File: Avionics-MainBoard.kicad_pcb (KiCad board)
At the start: 4 copper layers, 90.2 x 95.9 mm, 270 parts, among them J1 USB_C_Receptacle_USB2.0, J10 1824543, J11 1824527, J12 1824527, J13 1824527, J14 200528-0100, J15 200528-0100, J16 200528-0100, J17 1824543, J18 200528-0100, J19 200528-0100, J2 200528-0100, J3 Conn_01x06, J4 200528-0100, J5 Micro_SD_Card_Det2, J6 200528-0100, J7 U.FL-R-SMT-1, J8 Conn_01x02, J9 200528-0100, Q1 IRLML2803, Q10 MBT2222ADW1T1, Q11 MBT2222ADW1T1, Q12 MBT2222ADW1T1, Q13 MBT2222ADW1T1, Q14 MMBT2907, Q15 MMBT2907, Q16 NX3008NBKS, Q17 MBT2222ADW1T1, Q2 MBT2222ADW1T1, Q22 NX3008NBKS, Q24 NX3008NBKS, Q26 NX3008NBKS, Q28 NX3008NBKS, Q29 MBT2222ADW1T1, Q3 MBT2222ADW1T1, Q30 MBT2222ADW1T1, Q4 NX3008NBKS, Q44 NX3008NBKS, Q46 NX3008NBKS, Q48 NX3008NBKS, Q5 MBT2222ADW1T1, Q50 NX3008NBKS, Q52 NX3008NBKS, Q6 MBT2222ADW1T1, Q7 MBT2222ADW1T1, Q8 MBT2222ADW1T1, Q9 MBT2222ADW1T1, Q99 NX3008NBKS, SW1 SW_Omron_B3FS, SW2 SW_Omron_B3FS, U1 MR25H40MDF, U10 BTS5090-1EJA, U12 ADM1491EBR, U14 ADM1176-1ARMZ-R7, U15 TPS7A4501DCQT, U16 ADM1176-1ARMZ-R7, U17 TPS54226PWPR, U18 ADM1176-1ARMZ-R7, U2 RP2040, U3 MAX706RESA+, U4 DS3231M, U5 BNO085, U6 USBLC6-2SC6, U7 E22-900M30S, U8 S1216V8, U9 BQ25883RGER, Y1 12MHz, Y2 32.768kHz

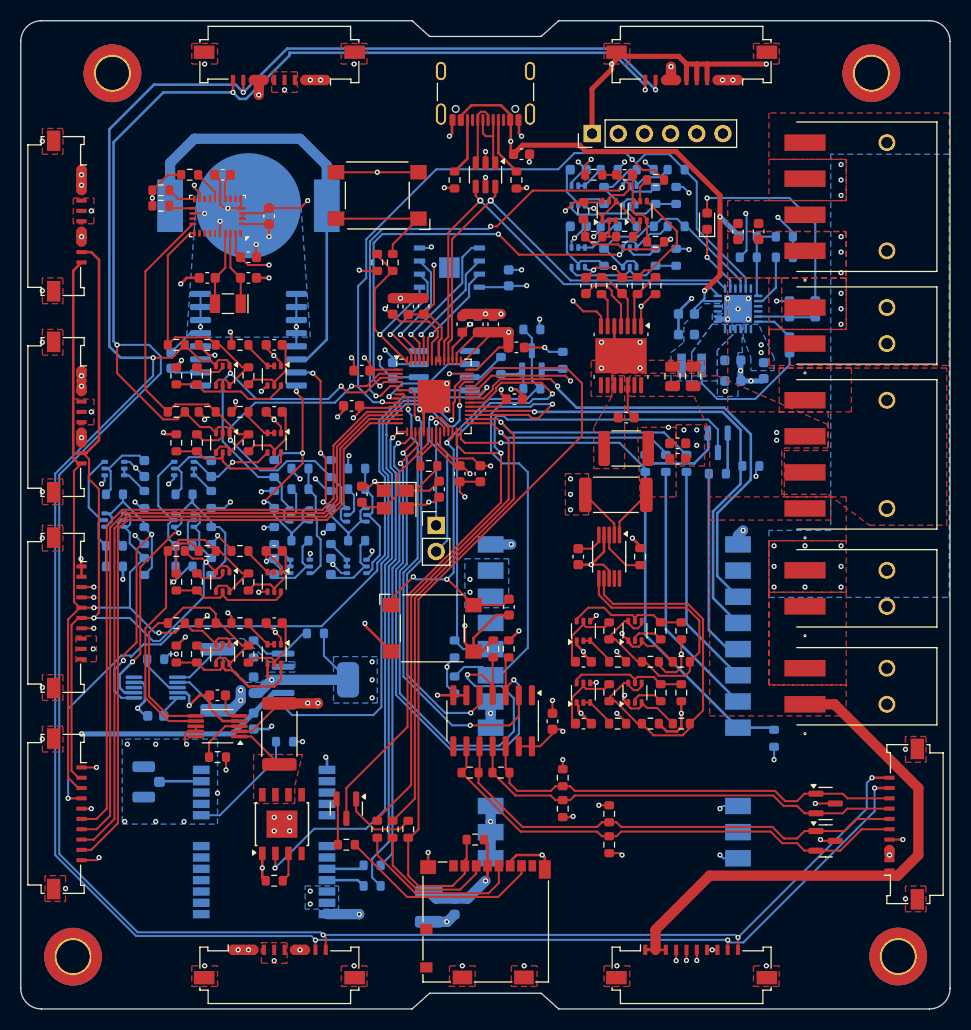
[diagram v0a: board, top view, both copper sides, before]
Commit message: Fixed schematic bugs and corresponding layout modifications
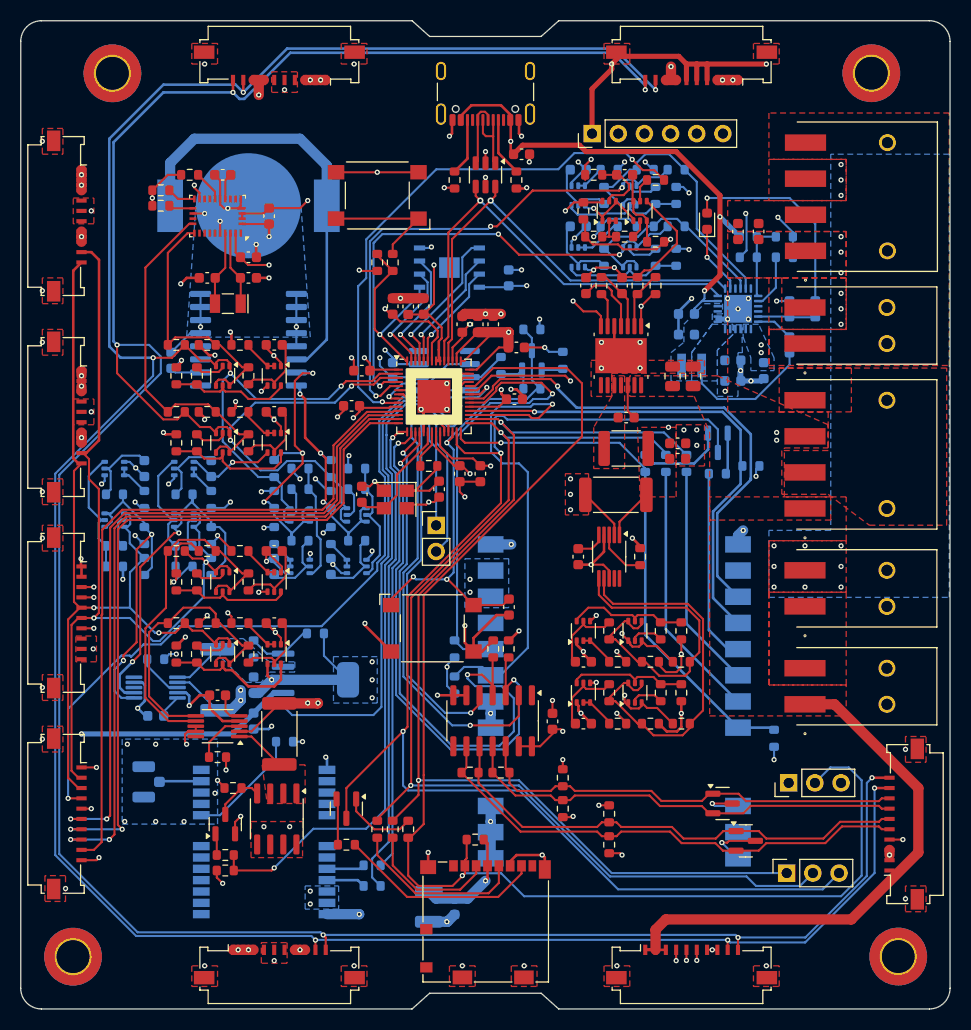
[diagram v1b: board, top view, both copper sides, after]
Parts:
- removed R64: 1k, Resistor_SMD:R_0603_1608Metric
- removed U10: BTS5090-1EJA, Package_SO:Infineon_PG-DSO-8-43
- added J20: Conn_01x03, Connector_PinSocket_2.54mm:PinSocket_1x03_P2.54mm_Vertical, F.Cu at (179.2, 134.8)
- added J21: Conn_01x03, Connector_PinHeader_2.54mm:PinHeader_1x03_P2.54mm_Vertical, F.Cu at (179.4, 126.0)
- added Q18: IRLML0030, Package_TO_SOT_SMD:SOT-23, F.Cu at (124.8, 130.0)
- added Q19: IRF7404, Package_SO:SOIC-8_3.9x4.9mm_P1.27mm, F.Cu at (129.8, 129.5)
- added R36: 10K, Resistor_SMD:R_0603_1608Metric, F.Cu at (124.8, 134.5)
- added R37: 4.7K, Resistor_SMD:R_0603_1608Metric, F.Cu at (124.8, 133.0)
- added R38: 3.3K, Resistor_SMD:R_0603_1608Metric, F.Cu at (125.5, 126.5)
- U4: value DS3231M -> DS3231S
- moved D1 10.0 mm to (173.0, 128.0)
- moved D2 7.75 mm to (175.2, 131.6)
- moved J10 0.05 mm to (181.1, 69.1)
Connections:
- J16 pad 6: /MCU_IO/SPI1_MISO -> /MCU_IO/Jetson_CSn
- J16 pad 7: /MCU_IO/Jetson_CSn -> /MCU_IO/SPI1_MOSI
- J16 pad 9: /MCU_IO/SPI1_MOSI -> /MCU_IO/SPI1_MISO
- J18 pad 10: /MCU_IO/I2C0_SDA -> /MCU_IO/I2C0_SCL
- J18 pad 9: /MCU_IO/I2C0_SCL -> /MCU_IO/I2C0_SDA
- J19 pad 10: /MCU_IO/I2C0_SDA -> /MCU_IO/I2C0_SCL
- J19 pad 9: /MCU_IO/I2C0_SCL -> /MCU_IO/I2C0_SDA
- J2 pad 10: /MCU_IO/I2C0_SDA -> /MCU_IO/I2C0_SCL
- J2 pad 9: /MCU_IO/I2C0_SCL -> /MCU_IO/I2C0_SDA
- J4 pad 10: /MCU_IO/I2C0_SDA -> /MCU_IO/I2C0_SCL
- J4 pad 9: /MCU_IO/I2C0_SCL -> /MCU_IO/I2C0_SDA
- J6 pad 10: /MCU_IO/I2C0_SDA -> /MCU_IO/I2C0_SCL
- J6 pad 9: /MCU_IO/I2C0_SCL -> /MCU_IO/I2C0_SDA
- Q17 pad 1: /MCU_IO/I2C0_SDA -> /MCU_IO/I2C0_SCL
- Q17 pad 3: /MCU_IO/I2C0_SDA -> /MCU_IO/I2C0_SCL
- Q17 pad 4: /RTC/RTC_SDA -> /RTC/RTC_SCL
- Q17 pad 6: /RTC/RTC_SDA -> /RTC/RTC_SCL
- Q3 pad 1: /MCU_IO/I2C0_SCL -> /MCU_IO/I2C0_SDA
- Q3 pad 3: /MCU_IO/I2C0_SCL -> /MCU_IO/I2C0_SDA
- Q5 pad 1: /MCU_IO/I2C0_SCL -> /MCU_IO/I2C0_SDA
- Q5 pad 3: /MCU_IO/I2C0_SCL -> /MCU_IO/I2C0_SDA
- Q5 pad 4: /RTC/RTC_SCL -> /RTC/RTC_SDA
- Q5 pad 6: /RTC/RTC_SCL -> /RTC/RTC_SDA
- Q9 pad 1: /MCU_IO/I2C0_SDA -> /MCU_IO/I2C0_SCL
- Q9 pad 3: /MCU_IO/I2C0_SDA -> /MCU_IO/I2C0_SCL
- R104 pad 1: /RTC/RTC_SDA -> /RTC/RTC_SCL
- R104 pad 2: /MCU_IO/I2C0_SDA -> /MCU_IO/I2C0_SCL
- R15 pad 2: /MCU_IO/I2C0_SDA -> /MCU_IO/I2C0_SCL
- R165 pad 2: /MCU_IO/I2C0_SCL -> /MCU_IO/I2C0_SDA
- R171 pad 1: /RTC/RTC_SCL -> /RTC/RTC_SDA
- R171 pad 2: /MCU_IO/I2C0_SCL -> /MCU_IO/I2C0_SDA
- R173 pad 2: /RTC/RTC_SCL -> /RTC/RTC_SDA
- R174 pad 1: /RTC/RTC_SCL -> /RTC/RTC_SDA
- R97 pad 2: /RTC/RTC_SDA -> /RTC/RTC_SCL
- R98 pad 1: /RTC/RTC_SDA -> /RTC/RTC_SCL
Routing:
- net /MCU_IO/SD_CSn: track 76.9 -> 132.4 mm, vias 0 -> 1
- net /LoRa Power/MISO: track 75.7 -> 128.1 mm, vias 1 -> 2
- net /LoRa Power/CLK: track 63.7 -> 107.3 mm, vias 1 -> 2
- net /LoRa Power/MOSI: track 66.6 -> 106.0 mm, vias 1 -> 2
- net /MCU_IO/I2C0_SCL: track 280.8 -> 291.2 mm
- net Net-(Q18-D): track 0.00 -> 4.95 mm
- net /MCU_IO/I2C0_SDA: track 287.7 -> 283.5 mm
- net /MCU_IO/GPS_EN: track 65.9 -> 70.0 mm
- net /RTC/RTC_SDA: track 26.8 -> 30.6 mm
- net GND: track 348.3 -> 351.8 mm, vias 127 -> 126
- net /MCU_IO/SPI1_CLK: track 67.2 -> 70.2 mm, vias 0 -> 2
- net Net-(U10-DEN): track 2.89 -> 0.00 mm
- net /MCU_IO/SPI1_MISO: track 66.3 -> 69.2 mm
- net Net-(Q18-G): track 0.00 -> 2.11 mm
- net /MCU_IO/SPI1_MOSI: track 67.9 -> 69.8 mm, vias 0 -> 2
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
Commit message: Updated connector locations and types
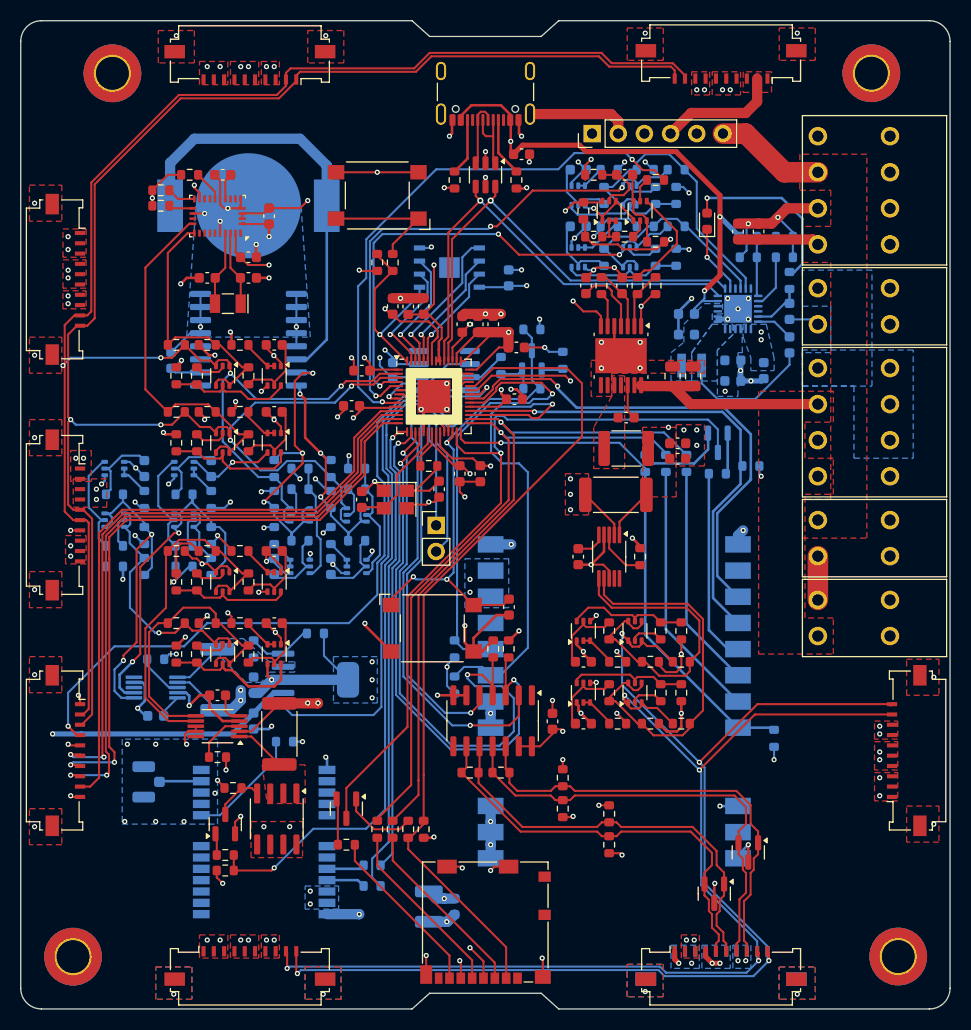
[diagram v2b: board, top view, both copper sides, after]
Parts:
- removed J20: Conn_01x03, Connector_PinSocket_2.54mm:PinSocket_1x03_P2.54mm_Vertical
- removed J21: Conn_01x03, Connector_PinHeader_2.54mm:PinHeader_1x03_P2.54mm_Vertical
- J10, J17: footprint Argus-Connectors:1824543 -> Argus-Connectors:1823654
- J11, J12, J13: footprint Argus-Connectors:1824527 -> Argus-Connectors:1823638
- J14: moved to B.Cu
- moved J14 95.8 mm to (172.9, 143.2), turned to 180 degrees
- moved J19 89.3 mm to (109.8, 77.1), turned to -90 degrees
- moved J2 86.4 mm to (127.1, 143.2), turned to 0 degrees
- moved J9 71.4 mm to (172.9, 56.8), turned to 180 degrees
- moved J18 63.7 mm to (190.4, 122.9), turned to 90 degrees
- moved J4 42.9 mm to (127.1, 56.8)
- moved J6 21.8 mm to (172.9, 143.2), turned to 0 degrees
- moved J15 9.50 mm to (109.8, 100.0)
- moved J16 6.14 mm to (109.8, 122.9)
- moved D2 5.96 mm to (172.2, 136.8), turned to -90 degrees
- moved D1 5.37 mm to (175.5, 132.8), turned to -90 degrees
- moved R48 5.10 mm to (144.0, 130.5), turned to -90 degrees
- moved J13 5.03 mm to (182.2, 111.8)
- moved R70 3.72 mm to (179.5, 77.2)
- moved J12 3.37 mm to (182.2, 104.0)
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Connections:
- J12 pad 3: GNDREF -> GND
- J12 pad 4: GNDREF -> GND
- J13 pad 3: GNDREF -> GND
- J13 pad 4: GNDREF -> GND
- J14 pad 1: VSYS -> /MCU_IO/I2C1_SCL
- J14 pad 10: /MCU_IO/I2C1_SCL -> VSYS
- J14 pad 2: VSYS -> /MCU_IO/I2C1_SDA
- J14 pad 3: VSYS -> +3V3
- J14 pad 4: GND -> +3V3
- J14 pad 7: +3V3 -> GND
- J14 pad 8: +3V3 -> VSYS
- J14 pad 9: /MCU_IO/I2C1_SDA -> VSYS
- J15 pad 5: /MCU_IO/I2C1_SCL -> /MCU_IO/I2C0_SCL
- J15 pad 6: /MCU_IO/I2C1_SDA -> /MCU_IO/I2C0_SDA
- J16 pad 2: /MCU_IO/I2C1_SDA -> /MCU_IO/I2C0_SDA
- J16 pad 3: /MCU_IO/I2C1_SCL -> /MCU_IO/I2C0_SCL
- J18 pad 10: /MCU_IO/I2C0_SCL -> /MCU_IO/I2C1_SCL
- J18 pad 9: /MCU_IO/I2C0_SDA -> /MCU_IO/I2C1_SDA
- J2 pad 10: /MCU_IO/I2C0_SCL -> /MCU_IO/I2C1_SCL
- J2 pad 9: /MCU_IO/I2C0_SDA -> /MCU_IO/I2C1_SDA
- J4 pad 1: VSYS -> /MCU_IO/I2C0_SCL
- J4 pad 10: /MCU_IO/I2C0_SCL -> VSYS
- J4 pad 2: VSYS -> /MCU_IO/I2C0_SDA
- J4 pad 3: VSYS -> +3V3
- J4 pad 4: GND -> +3V3
- J4 pad 7: +3V3 -> GND
- J4 pad 8: +3V3 -> VSYS
- J4 pad 9: /MCU_IO/I2C0_SDA -> VSYS
- J6 pad 10: /MCU_IO/I2C0_SCL -> /MCU_IO/I2C1_SCL
- J6 pad 9: /MCU_IO/I2C0_SDA -> /MCU_IO/I2C1_SDA
- J9 pad 10: /MCU_IO/I2C1_SCL -> /MCU_IO/I2C0_SCL
- J9 pad 9: /MCU_IO/I2C1_SDA -> /MCU_IO/I2C0_SDA
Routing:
- net /MCU_IO/I2C0_SCL: track 291.2 -> 176.2 mm, vias 8 -> 4
- net /MCU_IO/I2C0_SDA: track 283.5 -> 177.6 mm, vias 8 -> 4
- net /LoRa Power/MISO: track 128.1 -> 75.7 mm, vias 2 -> 1
- net /MCU_IO/SD_CSn: track 132.4 -> 81.0 mm, vias 1 -> 0
- net /MCU_IO/I2C1_SCL: track 213.1 -> 263.5 mm, vias 6 -> 8
- net VSYS: track 314.9 -> 364.1 mm, vias 15 -> 13
- net /LoRa Power/CLK: track 107.3 -> 63.7 mm, vias 2 -> 1
- net /LoRa Power/MOSI: track 106.0 -> 66.6 mm, vias 2 -> 1
- net /MCU_IO/I2C1_SDA: track 209.8 -> 238.5 mm, vias 6 -> 8
- net GND: track 351.8 -> 326.8 mm, vias 126 -> 129
- net +3V3: track 186.7 -> 172.7 mm, vias 66 -> 76
- net GNDREF: track 60.6 -> 47.4 mm, vias 17 -> 16
- net /MCU_IO/SPI1_MOSI: track 69.8 -> 62.1 mm
- net /RS485/TX+: track 48.9 -> 41.2 mm
- net /MCU_IO/SPI1_MISO: track 69.2 -> 61.7 mm
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- added copper zone on B.Cu, net +3V3
- added copper zone on B.Cu, net VSYS
- removed copper zone on F.Cu, net GNDREF
- removed copper zone on F.Cu, net Net-(J12-Pad1)
- removed copper zone on B.Cu, net VBATT

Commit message: Added silkscreen
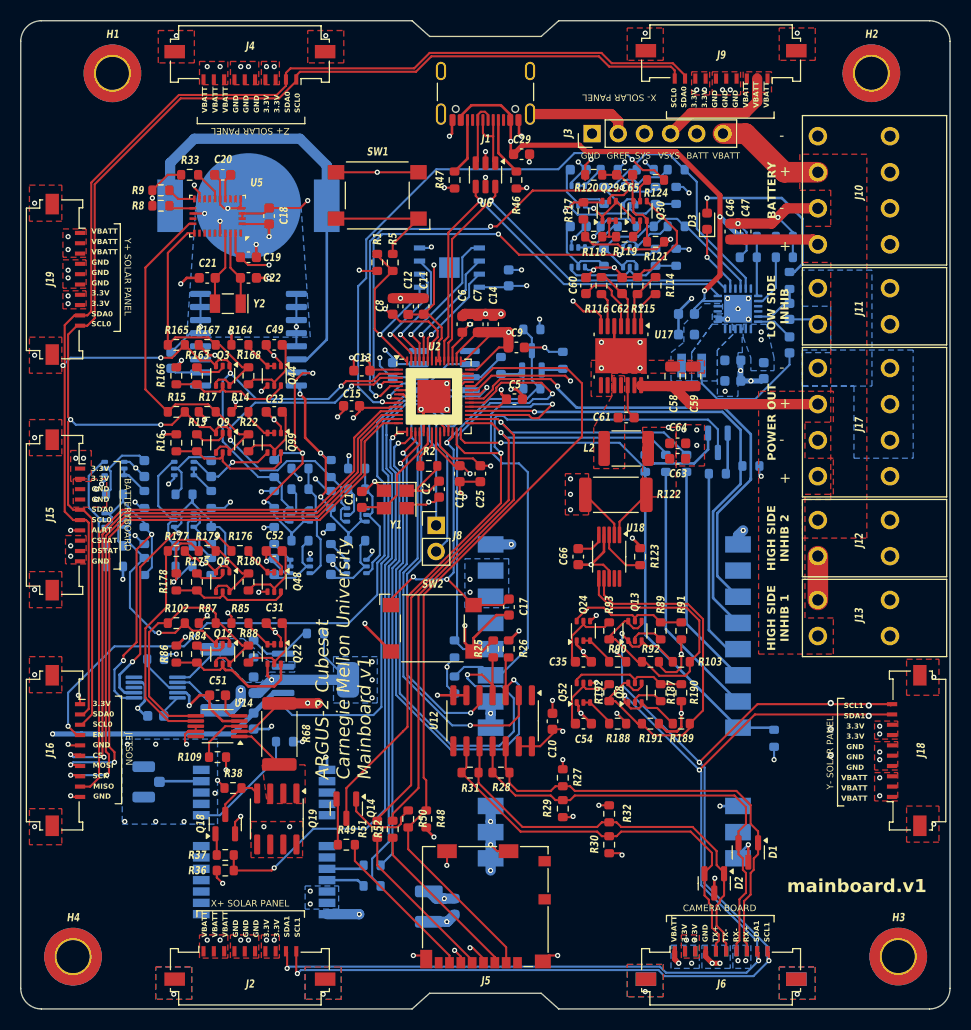
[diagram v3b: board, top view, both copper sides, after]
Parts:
- added REF**: VAL**, mainboard:board_info_block, B.Cu at (111.5, 77.5)
- moved J5 1.50 mm to (150.0, 138.0)
- moved C47 1.25 mm to (175.2, 72.5)
- moved R48 1.03 mm to (144.2, 129.5)
- moved D2 1.00 mm to (172.2, 135.8)
- moved R50 1.00 mm to (142.5, 129.5)
- moved C46 0.75 mm to (173.8, 72.5)
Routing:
- net /SD/SD_CLK: track 17.4 -> 15.7 mm
- net /SD/SD_MOSI: track 17.7 -> 16.2 mm
- net /SD/SD_MISO: track 16.8 -> 15.3 mm
- net +3V3: track 172.7 -> 171.4 mm
- net /MCU_IO/SD_CSn: track 81.0 -> 79.9 mm
- net GNDREF: track 47.4 -> 48.4 mm
- net VBATT: track 18.7 -> 19.5 mm
- net Net-(Q14-B): track 7.30 -> 7.90 mm
- net GND: track 326.8 -> 326.3 mm
- net /MCU_IO/I2C1_SCL: track 263.5 -> 263.0 mm, vias 8 -> 10
- net VSYS: vias 13 -> 14
- net /MCU_IO/I2C1_SDA: vias 8 -> 9
- net (no net): vias 0 -> 1
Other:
- board text added: "+"
- board text added: "-"
- board text added: "3.3V"
- board text added: "ALRT"
- board text added: "ARGUS-2 Cubesat Carnegie Mellon University Mainboard v1"
- board text added: "BATT"
- board text added: "BATTERY"
- board text added: "BATTERYBOARD"
- board text added: "CAMERA BOARD"
- board text added: "CS"
- board text added: "CSTAT"
- board text added: "DSTAT"
- board text added: "EN"
- board text added: "GND"
- board text added: "GREF"
- board text added: "HIGH SIDE INHIB 1"
- board text added: "HIGH SIDE INHIB 2"
- board text added: "JETSON"
- board text added: "LOW SIDE INHIB"
- board text added: "MISO"
- board text added: "MOSI"
- board text added: "POWER OUT"
- board text added: "RX+"
- board text added: "RX-"
- board text added: "SCK"
- board text added: "SCL0"
- board text added: "SCL1"
- board text added: "SDA0"
- board text added: "SDA1"
- board text added: "SYS"
- board text added: "TX+"
- board text added: "TX-"
- board text added: "VBATT"
- board text added: "VSYS"
- board text added: "X+ SOLAR PANEL"
- board text added: "X- SOLAR PANEL"
- board text added: "Y+ SOLAR PANEL"
- board text added: "Y- SOLAR PANEL"
- board text added: "Z+ SOLAR PANEL"
- board text added: "mainboard.v1"

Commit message: Minor fixes, export BOM
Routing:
- net GND: track 326.3 -> 320.8 mm
- net +3V3: track 171.4 -> 167.0 mm
- net /MCU_IO/I2C0_SCL: track 176.2 -> 180.3 mm
- net GNDREF: track 48.4 -> 45.8 mm
- net /MCU_IO/I2C0_SDA: track 177.6 -> 179.9 mm
- net Net-(Q4B-G): track 7.68 -> 8.95 mm
- net /MCU_IO/I2C1_SCL: track 263.0 -> 264.2 mm, vias 10 -> 8
- net /MCU_IO/RS485_RX_EN: track 52.5 -> 51.4 mm
- net Net-(C2-Pad2): track 8.50 -> 7.40 mm
- net /USB/VUSB: track 55.0 -> 53.9 mm
- net /MCU_IO/UART1_TX: track 39.6 -> 38.5 mm
- net GPS_VDD: track 40.5 -> 41.5 mm
- net Net-(U15-OUT): track 5.01 -> 6.08 mm
- net LoRa_VDD: track 46.8 -> 47.9 mm
- net Net-(U14-VCC): track 5.01 -> 6.08 mm
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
